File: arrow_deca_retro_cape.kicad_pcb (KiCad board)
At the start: 4 copper layers, 78.6 x 97.7 mm, 47 parts, among them J1 ZXSP_ED2X28_SPE_SOL_EDGE, J10 Conn_02x05_Odd_Even, J11 Conn_01x04, J12 Conn_01x03, J13 Conn_01x01, J14 Conn_01x02, J15 Conn_01x03, J2 Conn_01x03, J3 Conn_01x03, J4 DB9_Male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

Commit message: added Deto pmod
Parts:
- added J16: Conn_01x06, Connector_PinHeader_2.54mm:PinHeader_1x06_P2.54mm_Vertical, F.Cu at (141.9, 118.1)
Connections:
- J1 pad A27: unconnected-(J1-PadA27) -> /DETO4
- J1 pad B10: unconnected-(J1-PadB10) -> /JOY1_B1_P6
- J1 pad B11: unconnected-(J1-PadB11) -> /JOY1_DOWN
- J1 pad B12: unconnected-(J1-PadB12) -> /JOY1_B2_P9
- J1 pad B2: unconnected-(J1-PadB2) -> /PS2_MOUSE_DAT
- J1 pad B24: unconnected-(J1-PadB24) -> +2V5
- J1 pad B26: unconnected-(J1-PadB26) -> /PS2_MOUSE_CLK
- J1 pad B3: unconnected-(J1-PadB3) -> /DETO3
- J1 pad B6: unconnected-(J1-PadB6) -> /JOY1_RIGHT
- J1 pad B7: unconnected-(J1-PadB7) -> /JOY1_LEFT
- J1 pad B8: unconnected-(J1-PadB8) -> /JOY1_UP
- J1 pad B9: unconnected-(J1-PadB9) -> /JOYX_SEL_O
- J5 pad 1: /PS2_DATA -> /PS2_KEYB_DAT
- J9 pad 12: /PS2_KEYB_CLK -> /PS2_KEYB_DAT
- R1 pad 1: /PS2_KEYB_DATA -> /PS2_KEYB_DAT
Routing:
- net /PS2_KEYB_CLK: track 69.3 -> 38.2 mm
- net /PS2_KEYB_DAT: track 0.00 -> 31.2 mm
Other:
- board text added: "1"
- board text added: "2"
- board text added: "3"
- board text added: "4"
- board text added: "DETO PMOD"

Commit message: v0.5 routing finalized
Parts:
- added C21: 100uF, Capacitor_SMD:C_0805_2012Metric_Pad1.18x1.45mm_HandSolder, F.Cu at (140.2, 99.1)
- added LO1: KiCad-Logo2_12mm_SilkScreen, Symbol:KiCad-Logo2_12mm_SilkScreen, B.Cu at (143.3, 75.0)
- added LO2: OSHW-Logo2_9.8x8mm_SilkScreen, Symbol:OSHW-Logo2_9.8x8mm_SilkScreen, F.Cu at (137.2, 75.9)
- added LO3: OSHW-Logo2_14.6x12mm_SilkScreen, Symbol:OSHW-Logo2_14.6x12mm_SilkScreen, B.Cu at (143.5, 105.4)
- added LO4: ESD-Logo_6.6x6mm_SilkScreen, Symbol:ESD-Logo_6.6x6mm_SilkScreen, B.Cu at (142.0, 135.8)
- C20: value 0.1uF -> 10uF
- J11: value Conn_01x04 -> USB_A; footprint Connector_PinSocket_2.54mm:PinSocket_1x04_P2.54mm_Vertical -> Connector_USB:USB_A_Molex_67643_Horizontal
- moved J11 7.16 mm to (157.5, 49.3), turned to 180 degrees
- moved D1 4.82 mm to (142.8, 45.7), turned to 90 degrees
- moved R3 3.85 mm to (161.2, 53.1)
- moved R4 3.64 mm to (161.2, 55.1)
- moved R2 3.03 mm to (142.9, 42.5)
- moved J5 2.54 mm to (131.7, 39.8)
- moved R1 2.33 mm to (142.9, 53.3)
- moved J1 2.30 mm to (107.1, 111.6)
- moved D2 1.72 mm to (142.8, 50.1), turned to 90 degrees
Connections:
- D1 pad 3: Net-(D1-Pad3) -> /USB_D-_DM
- D2 pad 3: Net-(D2-Pad3) -> /USB_D+_DP
- J11 pad 2: Net-(D2-Pad3) -> /USB_D-_DM
- J11 pad 3: Net-(D1-Pad3) -> /USB_D+_DP
- R1 pad 1: /PS2_KEYB_DAT -> /PS2_KEYB_CLK
- R1 pad 2: Net-(D2-Pad3) -> /USB_D+_DP
- R2 pad 1: /PS2_KEYB_CLK -> /PS2_KEYB_DAT
- R2 pad 2: Net-(D1-Pad3) -> /USB_D-_DM
- R3 pad 1: Net-(D1-Pad3) -> /USB_D-_DM
- R4 pad 1: Net-(D2-Pad3) -> /USB_D+_DP
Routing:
- net /DETO4: track 0.00 -> 213.3 mm, vias 0 -> 1
- net /UART_RXD: track 8.96 -> 182.8 mm, vias 0 -> 1
- net /SPI_CS_IO: track 0.00 -> 160.1 mm, vias 0 -> 2
- net /DETO2: track 0.00 -> 103.2 mm, vias 0 -> 2
- net /DETO1: track 0.00 -> 101.7 mm, vias 0 -> 2
- net /SPI_CS_FPGA: track 0.00 -> 76.5 mm, vias 0 -> 3
- net GND: track 535.1 -> 610.1 mm, vias 20 -> 22
- net /SPI_CS_OSD: track 0.00 -> 73.6 mm, vias 0 -> 1
- net /UART_TXD: track 14.9 -> 87.1 mm, vias 0 -> 1
- net +2V5: track 58.7 -> 130.6 mm, vias 1 -> 2
- net /SPI_DI (MISO): track 0.00 -> 62.3 mm, vias 0 -> 3
- net /PS2_MOUSE_DAT: track 0.00 -> 61.0 mm, vias 0 -> 1
- net /DETO3: track 0.00 -> 57.6 mm
- net +5V: track 150.3 -> 198.5 mm, vias 1 -> 3
- net /VGA_B0: track 0.00 -> 44.3 mm
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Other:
- board size 78.6 x 97.7 mm -> 78.6 x 100 mm
- board text added: "0.1270 mm"
- board text added: "0.1270 mm / 0.0000 mm"
- board text added: "1.6000 mm"
- board text added: "3P DUAL"
- board text added: "78.6332 mm x 100.0130 mm"
- board text added: "BOARD CHARACTERISTICS"
- board text added: "Board Thickness:"
- board text added: "Board overall dimensions:"
- board text added: "Castellated pads:"
- board text added: "Copper Finish:"
- board text added: "Copper Layer Count:"
- board text added: "DB9 (2V5 MAX!!!)"
- board text added: "DECA Retro Cape 1 v${VERSION}"
- board text added: "Edge card connectors:"
- board text added: "Impedance Control:"
- board text added: "MISTER MODULE"
- board text added: "Min hole diameter:"
- board text added: "Min track/spacing:"
- board text added: "No"
- board text added: "None"
- board text added: "PS2 Keyb. 3V3"
- board text added: "Plated Board Edge:"
- board text added: "SDRAM SELECT"
- board text added: "UART"
- board text added: "created by Hard Team Deca Somhic & Rhoderik & C.Palmero (PCB adapted from Tom Verbeure)"
- board text added: "https://github.com/somhi/DECA_retro_cape_1"
- board text removed: "Arrow DECA Retro Cape Somhic (adapted from Tom Verbeure) https://github.com/somhi/xxxx"
- board text removed: "Keyb.3V3"

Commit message: update before split
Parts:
- removed J11: USB_A, Connector_USB:USB_A_Molex_67643_Horizontal
- R1, R2: value 510 -> 120
- R3, R4: value 4k7 -> NC
- moved LO2 38.4 mm to (141.7, 114.0)
- moved LO4 28.4 mm to (119.4, 118.6)
- moved J16 15.2 mm to (141.6, 133.3), turned to 180 degrees
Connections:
- D1 pad 3: /USB_D-_DM -> Net-(D1-Pad3)
- D2 pad 3: /USB_D+_DP -> Net-(D2-Pad3)
- J5 pad 1: /PS2_KEYB_DAT -> Net-(D1-Pad3)
- J5 pad 4: +3V3 -> +5V
- J5 pad 5: /PS2_KEYB_CLK -> Net-(D2-Pad3)
- R1 pad 2: /USB_D+_DP -> Net-(D2-Pad3)
- R2 pad 2: /USB_D-_DM -> Net-(D1-Pad3)
- R3 pad 1: /USB_D-_DM -> Net-(D1-Pad3)
- R4 pad 1: /USB_D+_DP -> Net-(D2-Pad3)
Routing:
- net Net-(D2-Pad3): track 0.00 -> 44.3 mm
- net Net-(D1-Pad3): track 0.00 -> 41.2 mm
- net /USB_D+_DP: track 25.4 -> 0.00 mm
- net /USB_D-_DM: track 23.4 -> 0.00 mm
- net /DETO1: track 101.7 -> 118.6 mm
- net +3V3: track 281.4 -> 294.3 mm
- net GND: track 610.1 -> 622.5 mm
- net /DETO2: track 103.2 -> 113.9 mm
- net /DETO4: track 213.3 -> 218.8 mm
- net /DETO3: track 57.6 -> 62.6 mm
- net /UART_RXD: track 182.8 -> 184.0 mm
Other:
- board text added: "EDGE MIDI2SBC: PMOD1/2 VGA PMOD, PMOD3 SPI+UART, PMOD4 AIN BEWARE: DO NOT SUPPLY 3V3 INTO PMOD4 (MAX. 2V5 !!!!)"
- board text removed: "D+"
- board text removed: "D-"
- board text removed: "MIDI2SBC PMOD1/2 VGA PMOD, PMOD3 SPI+UART, PMOD4 AIN (MAX. 2V5 !!!!) BEWARE: DO NOT SUPPLY 3V3 INTO PMOD4"

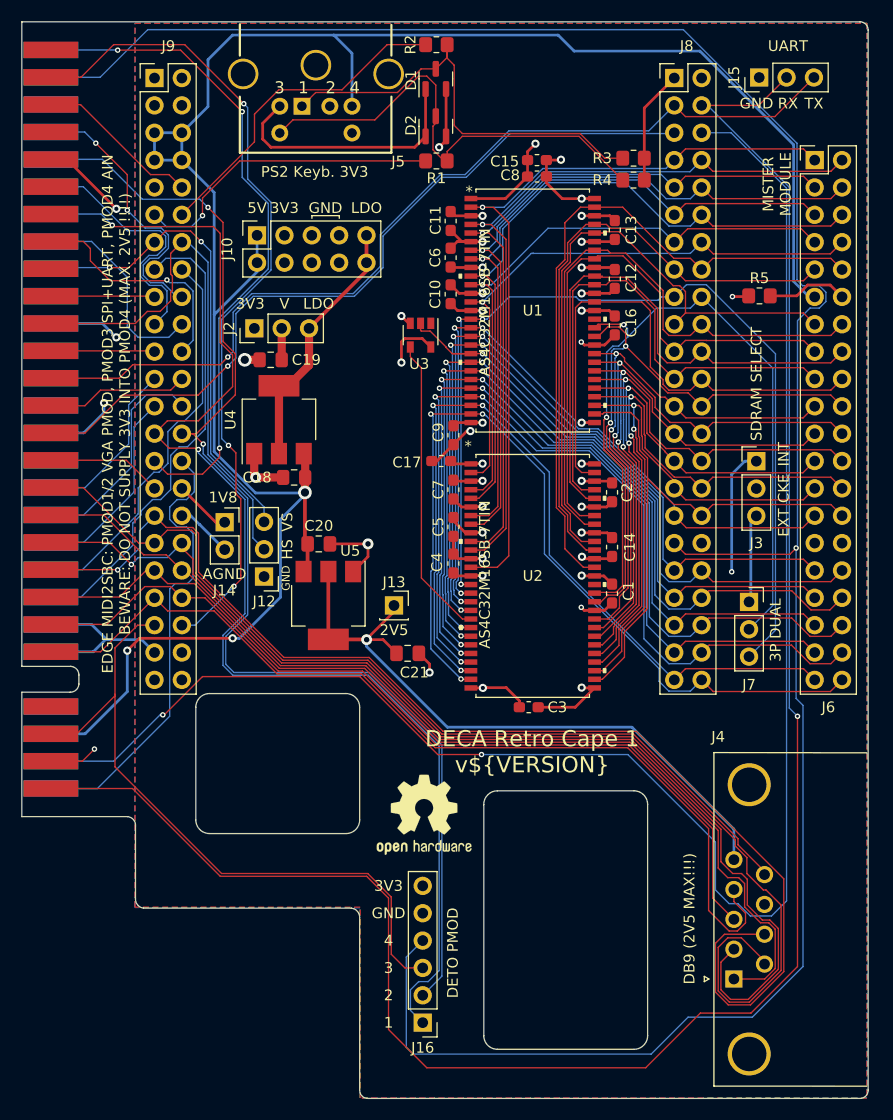
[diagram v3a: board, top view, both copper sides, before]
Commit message: v0.6 embedded SDRAM only version
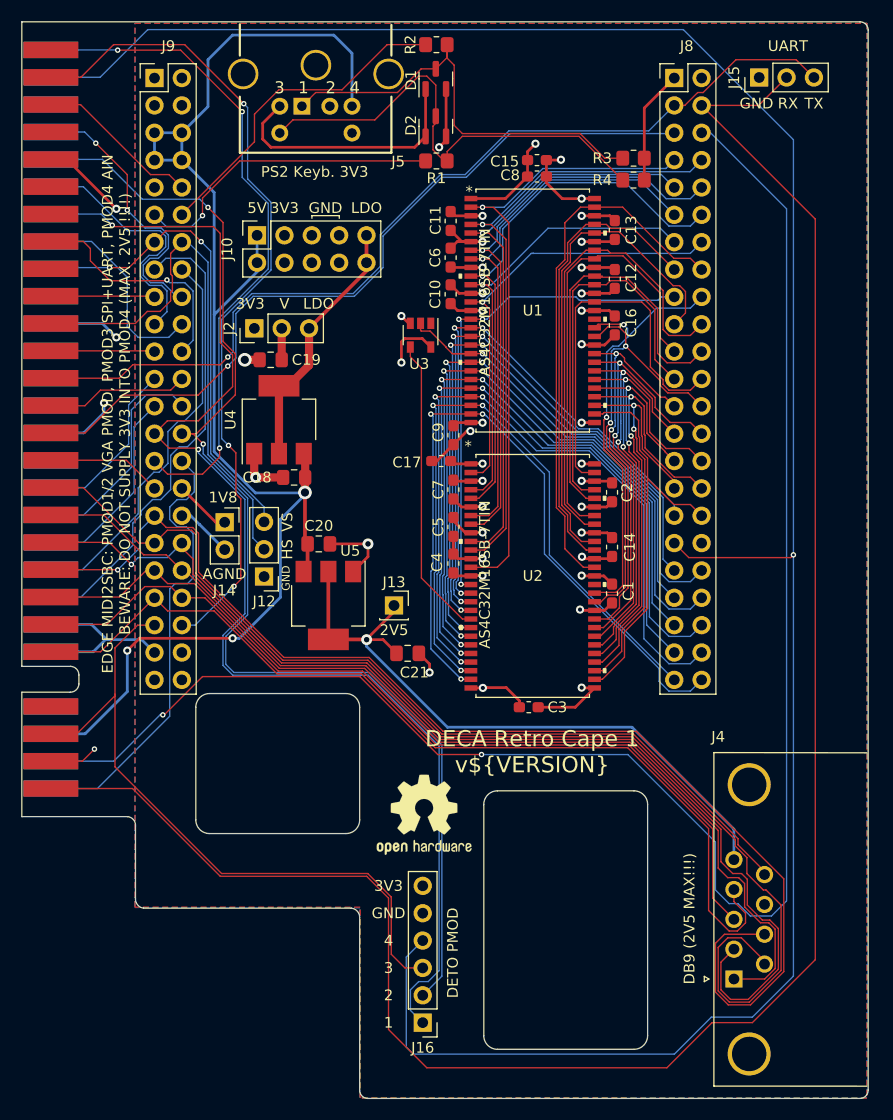
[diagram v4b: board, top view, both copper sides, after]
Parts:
- removed J3: Conn_01x03, Connector_PinHeader_2.54mm:PinHeader_1x03_P2.54mm_Vertical
- removed J6: Conn_02x20_Odd_Even, Connector_PinHeader_2.54mm:PinHeader_2x20_P2.54mm_Vertical
- removed J7: Conn_01x03, Connector_PinSocket_2.54mm:PinSocket_1x03_P2.54mm_Vertical
- removed R5: 10k, Resistor_SMD:R_0805_2012Metric_Pad1.20x1.40mm_HandSolder
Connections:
- C1 pad 1: /CKE_INT -> +3V3
- C16 pad 1: /CKE_INT -> +3V3
- U1 pad 37: /CKE_INT -> +3V3
- U2 pad 37: /CKE_INT -> +3V3
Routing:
- net /CKE_INT: track 67.2 -> 0.00 mm, vias 4 -> 0
- net +5V: track 198.2 -> 136.0 mm
- net GND: track 622.5 -> 565.6 mm
- net /LDQM: track 88.4 -> 46.7 mm
- net /UDQM: track 75.0 -> 40.5 mm
- net /BA0: track 79.5 -> 65.0 mm
- net /A1: track 83.8 -> 69.3 mm
- net /A10: track 81.5 -> 67.0 mm
- net /DQ6: track 56.8 -> 42.7 mm
- net /nWE: track 68.4 -> 54.4 mm
- net /A7: track 53.1 -> 39.2 mm
- net /A3: track 82.3 -> 68.3 mm
- net /DQ7: track 55.2 -> 41.3 mm
- net /A12: track 51.2 -> 37.2 mm
- net /A9: track 51.5 -> 37.6 mm
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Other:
- board text removed: "3P DUAL"
- board text removed: "CKE"
- board text removed: "EXT"
- board text removed: "INT"
- board text removed: "MISTER MODULE"
- board text removed: "SDRAM SELECT"
